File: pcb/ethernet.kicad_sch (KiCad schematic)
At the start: 39 parts, among them J6 RJ45_Hanrun_HR911105A_Horizon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, U7 W5500, Y1 Crystal_GND24

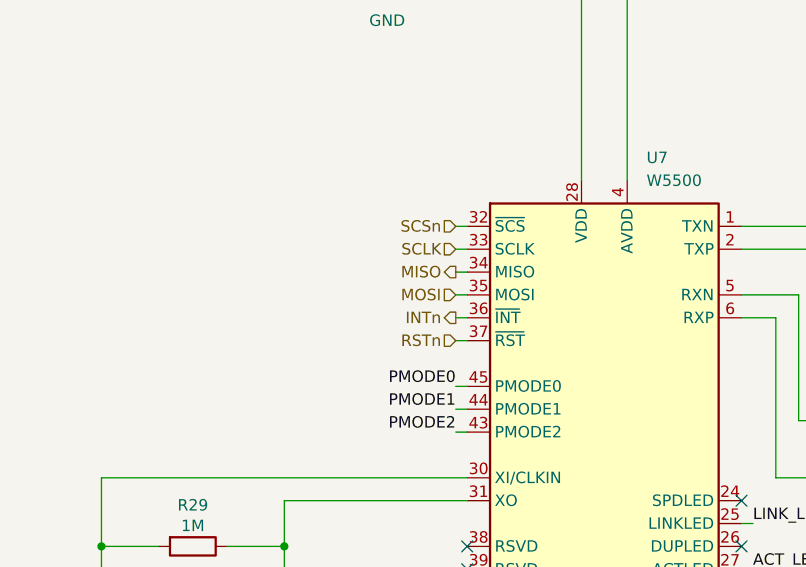
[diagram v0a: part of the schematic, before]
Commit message: feat: connect ethernet to mcu and sort erc errors
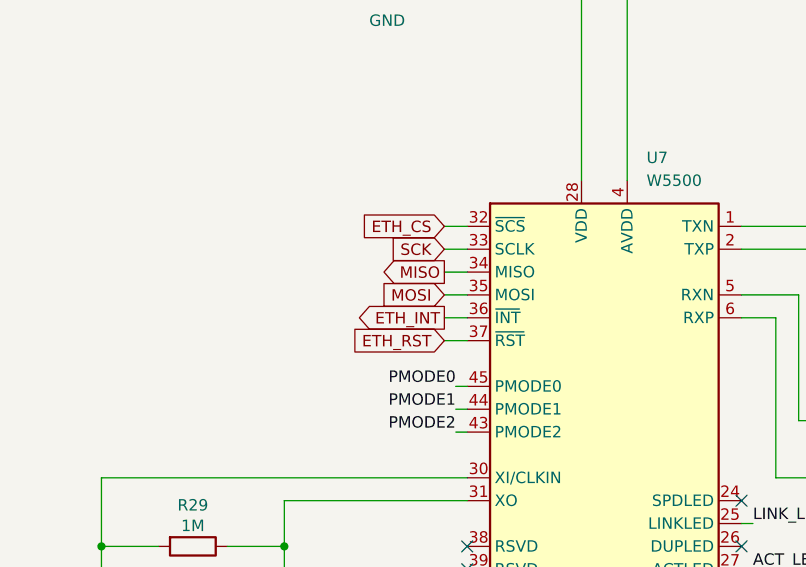
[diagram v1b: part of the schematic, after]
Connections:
- net INTn renamed ETH_INT
- net RSTn renamed ETH_RST
- net SCLK renamed SCK
- net SCSn renamed ETH_CS
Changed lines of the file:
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@@
-	(wire
-		(pts
-			(xy 67.31 76.2) (xy 68.58 76.2)
-		)
-		(stroke
-			(width 0)
-			(type default)
-		)
-	)
-	(wire
-		(pts
-			(xy 67.31 81.28) (xy 68.58 81.28)
-		)
-		(stroke
-			(width 0)
-			(type default)
-		)
-	)
 	(wire
 		(pts
@@
 	(wire
 		(pts
-			(xy 67.31 71.12) (xy 68.58 71.12)
-		)
-		(stroke
-			(width 0)
-			(type default)
-		)
-	)
-	(wire
-		(pts
 			(xy 132.08 173.99) (xy 133.35 173.99)
 		)
@@
 	(wire
 		(pts
+			(xy 66.04 78.74) (xy 68.58 78.74)
+		)
+		(stroke
+			(width 0)
+			(type default)
+		)
+	)
+	(wire
+		(pts
 			(xy 129.54 96.52) (xy 133.35 96.52)
 		)
@@
 	(wire
 		(pts
+			(xy 66.04 73.66) (xy 68.58 73.66)
+		)
+		(stroke
+			(width 0)
+			(type default)
+		)
+	)
+	(wire
+		(pts
 			(xy 86.36 29.21) (xy 86.36 63.5)
 		)
@@
 	(wire
 		(pts
-			(xy 67.31 78.74) (xy 68.58 78.74)
-		)
-		(stroke
-			(width 0)
-			(type default)
-		)
-	)
-	(wire
-		(pts
 			(xy 134.62 38.1) (xy 134.62 39.37)
 		)
@@
 	(wire
 		(pts
+			(xy 66.04 68.58) (xy 68.58 68.58)
+		)
+		(stroke
+			(width 0)
+			(type default)
+		)
+	)
+	(wire
+		(pts
+			(xy 66.04 71.12) (xy 68.58 71.12)
+		)
+		(stroke
+			(width 0)
+			(type default)
+		)
+	)
+	(wire
+		(pts
 			(xy 134.62 39.37) (xy 121.92 39.37)
 		)
@@
 	(wire
 		(pts
+			(xy 66.04 76.2) (xy 68.58 76.2)
+		)
+		(stroke
+			(width 0)
+			(type default)
+		)
+	)
+	(wire
+		(pts
 			(xy 99.06 101.6) (xy 100.33 101.6)
 		)
@@
 	(wire
 		(pts
-			(xy 67.31 68.58) (xy 68.58 68.58)
-		)
-		(stroke
-			(width 0)
-			(type default)
-		)
-	)
-	(wire
-		(pts
 			(xy 241.3 71.12) (xy 246.38 71.12)
 		)
@@
 	(wire
 		(pts
-			(xy 67.31 73.66) (xy 68.58 73.66)
-		)
-		(stroke
-			(width 0)
-			(type default)
-		)
-	)
-	(wire
-		(pts
 			(xy 111.76 128.27) (xy 111.76 129.54)
 		)
@@
 		(pts
 			(xy 144.78 55.88) (xy 144.78 57.15)
+		)
+		(stroke
+			(width 0)
+			(type default)
+		)
+	)
+	(wire
+		(pts
+			(xy 66.04 81.28) (xy 68.58 81.28)
 		)
 		(stroke
@@
 		)
 	)
-	(hierarchical_label "INTn"
+	(global_label "MISO"
 		(shape output)
-		(at 67.31 78.74 180)
+		(at 66.04 73.66 180)
+		(fields_autoplaced yes)
 		(effects
 			(font
@@
 			(justify right)
 		)
-	)
-	(hierarchical_label "SCSn"
+		(property "Intersheetrefs" "${INTERSHEET_REFS}"
+			(at 58.4586 73.66 0)
+			(hide yes)
+			(show_name no)
+			(do_not_autoplace no)
+			(effects
+				(font
+					(size 1.27 1.27)
+				)
+				(justify right)
+			)
+		)
+	)
+	(global_label "ETH_RST"
 		(shape input)
-		(at 67.31 68.58 180)
+		(at 66.04 81.28 180)
+		(fields_autoplaced yes)
 		(effects
 			(font
@@
 			(justify right)
 		)
-	)
-	(hierarchical_label "MISO"
-		(shape output)
-		(at 67.31 73.66 180)
+		(property "Intersheetrefs" "${INTERSHEET_REFS}"
+			(at 55.193 81.28 0)
+			(hide yes)
+			(show_name no)
+			(do_not_autoplace no)
+			(effects
+				(font
+					(size 1.27 1.27)
+				)
+				(justify right)
+			)
+		)
+	)
+	(global_label "MOSI"
+		(shape input)
+		(at 66.04 76.2 180)
+		(fields_autoplaced yes)
 		(effects
 			(font
@@
 			(justify right)
 		)
-	)
-	(hierarchical_label "SCLK"
+		(property "Intersheetrefs" "${INTERSHEET_REFS}"
+			(at 58.4586 76.2 0)
+			(hide yes)
+			(show_name no)
+			(do_not_autoplace no)
+			(effects
+				(font
+					(size 1.27 1.27)
+				)
+				(justify right)
+			)
+		)
+	)
+	(global_label "ETH_CS"
 		(shape input)
-		(at 67.31 71.12 180)
+		(at 66.04 68.58 180)
+		(fields_autoplaced yes)
 		(effects
 			(font
@@
 			(justify right)
 		)
-	)
-	(hierarchical_label "MOSI"
+		(property "Intersheetrefs" "${INTERSHEET_REFS}"
+			(at 56.1606 68.58 0)
+			(hide yes)
+			(show_name no)
+			(do_not_autoplace no)
+			(effects
+				(font
+					(size 1.27 1.27)
+				)
+				(justify right)
+			)
+		)
+	)
+	(global_label "SCK"
 		(shape input)
-		(at 67.31 76.2 180)
+		(at 66.04 71.12 180)
+		(fields_autoplaced yes)
 		(effects
 			(font
@@
 			(justify right)
 		)
-	)
-	(hierarchical_label "RSTn"
-		(shape input)
-		(at 67.31 81.28 180)
+		(property "Intersheetrefs" "${INTERSHEET_REFS}"
+			(at 59.3053 71.12 0)
+			(hide yes)
+			(show_name no)
+			(do_not_autoplace no)
+			(effects
+				(font
+					(size 1.27 1.27)
+				)
+				(justify right)
+			)
+		)
+	)
+	(global_label "ETH_INT"
+		(shape output)
+		(at 66.04 78.74 180)
+		(fields_autoplaced yes)
 		(effects
 			(font
@@
 			(justify right)
 		)
-	)
+		(property "Intersheetrefs" "${INTERSHEET_REFS}"
+			(at 55.7372 78.74 0)
+			(hide yes)
+			(show_name no)
+			(do_not_autoplace no)
+			(effects
+				(font
+					(size 1.27 1.27)
+				)
+				(justify right)
+			)
+		)
+	)

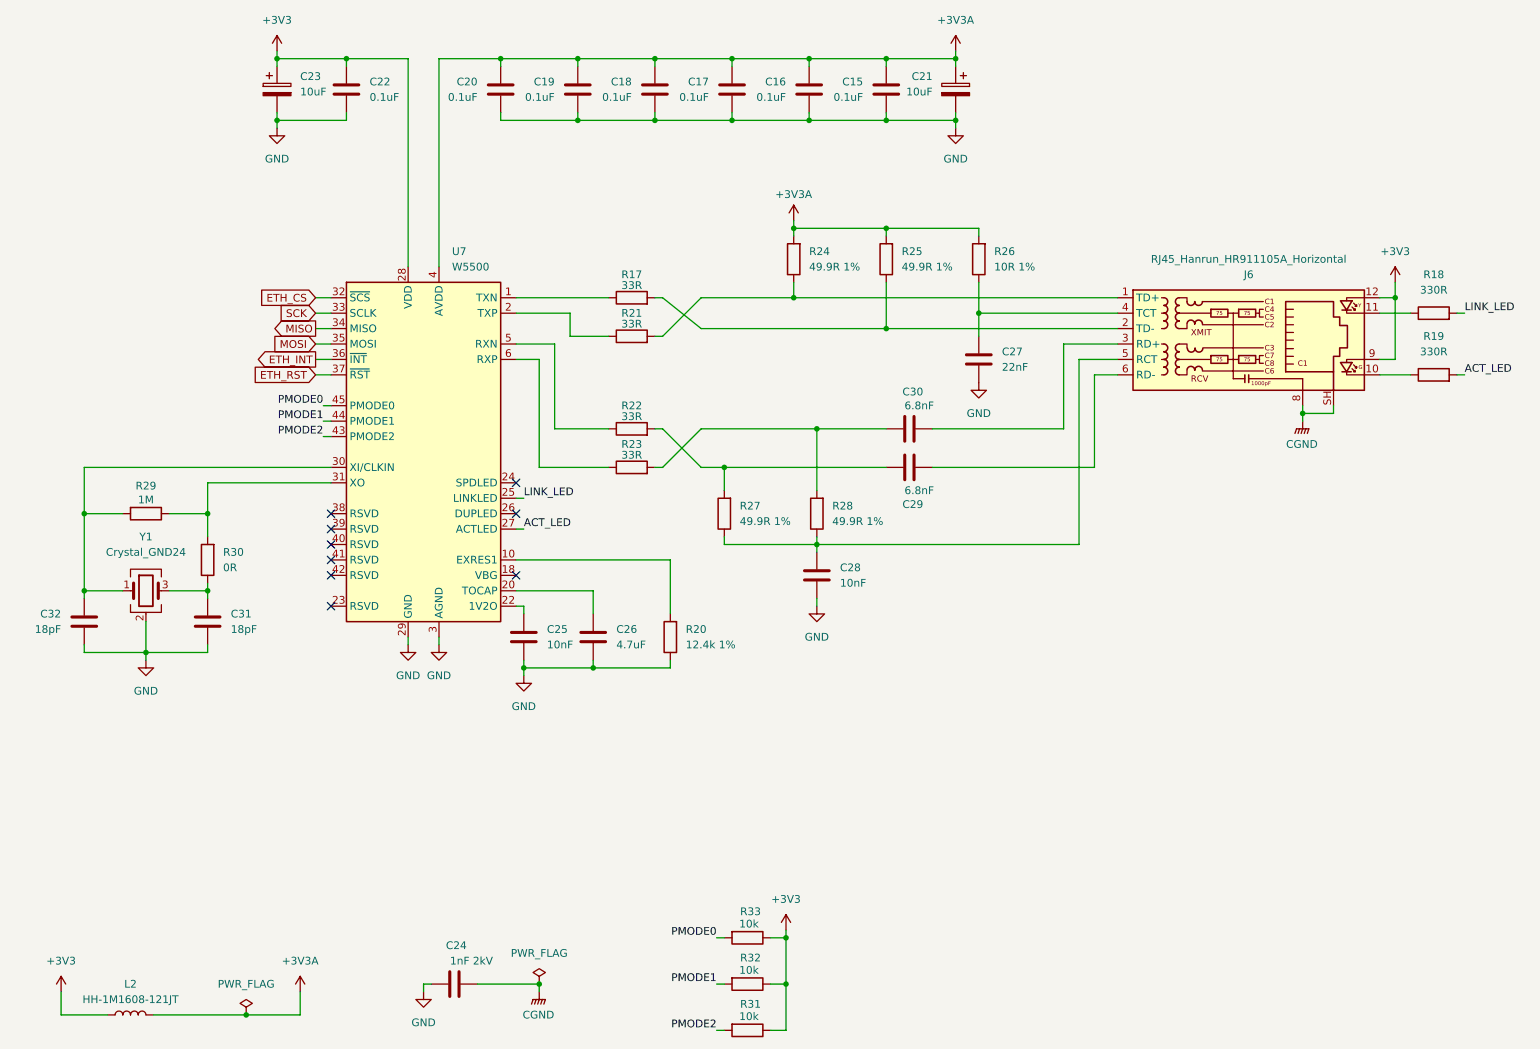
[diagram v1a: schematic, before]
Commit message: feat: update compoents with lcsc parts
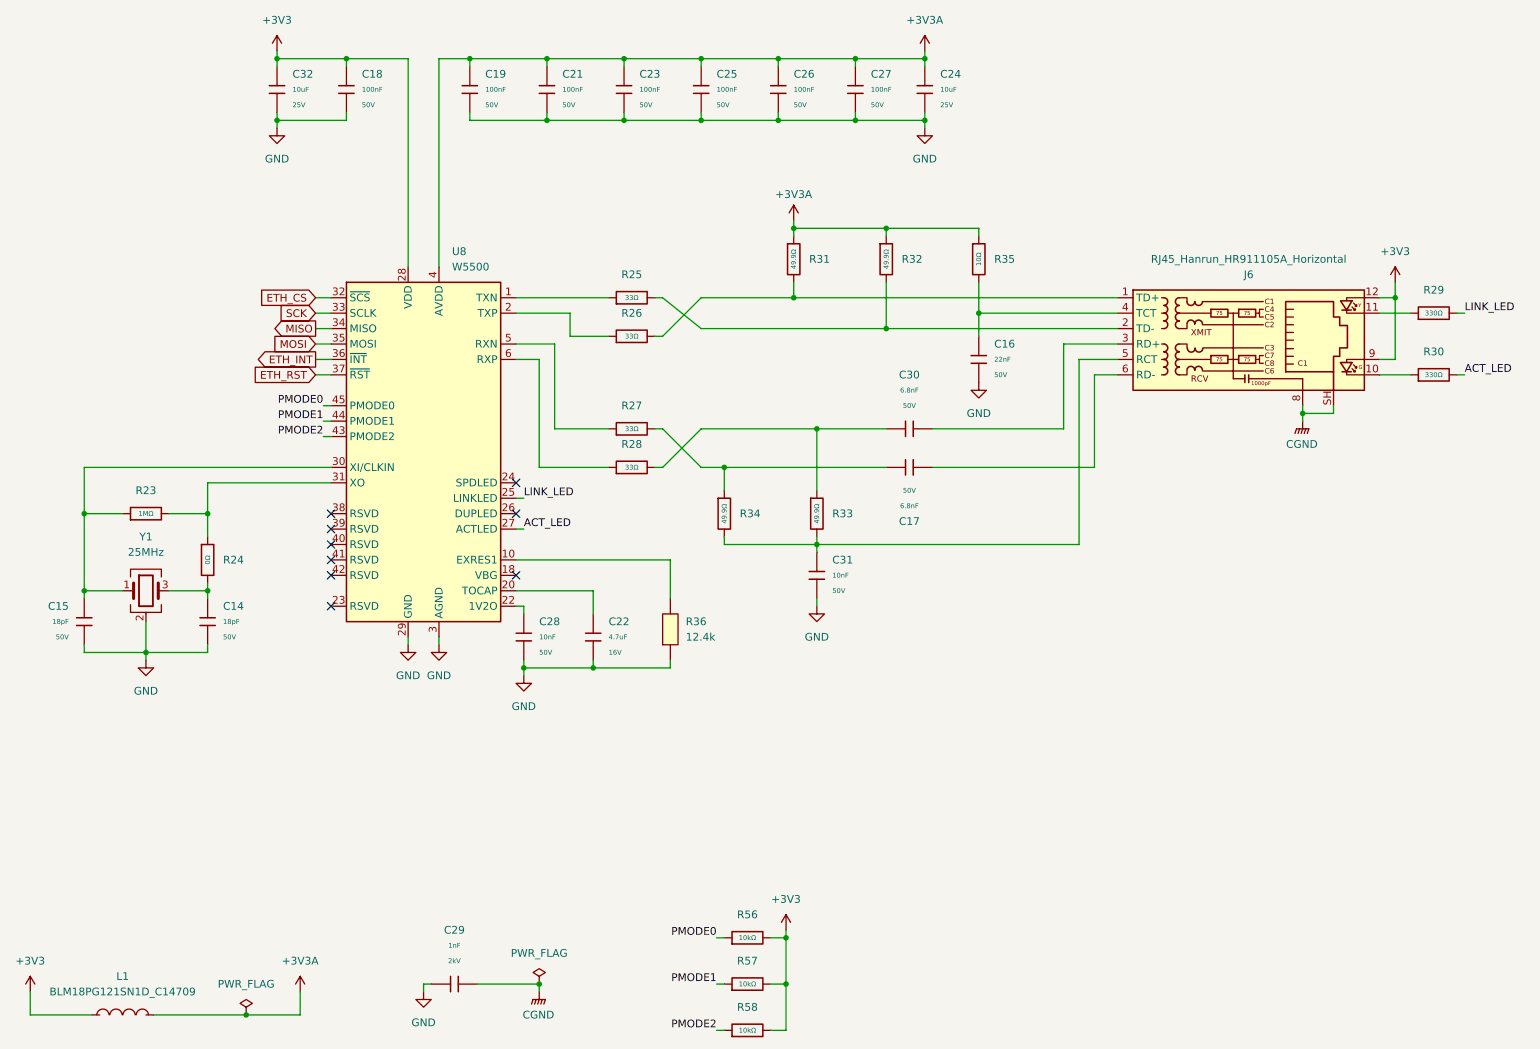
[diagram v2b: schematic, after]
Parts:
- removed C15, C16, C17, C18, C19, C20, C22: 0.1uF, symbol Device:C
- removed C21, C23: 10uF, symbol Device:C_Polarized
- removed C24: 1nF 2kV, symbol Device:C
- removed C25, C28: 10nF, symbol Device:C
- removed C26: 4.7uF, symbol Device:C
- removed C27: 22nF, symbol Device:C
- removed C29, C30: 6.8nF, symbol Device:C
- removed C31, C32: 18pF, symbol Device:C
- removed L2: HH-1M1608-121JT, symbol Device:L
- removed R17, R21, R22, R23: 33R, symbol Device:R
- removed R18, R19: 330R, symbol Device:R
- removed R20: 12.4k 1%, symbol Device:R
- removed R24, R25, R27, R28: 49.9R 1%, symbol Device:R
- removed R26: 10R 1%, symbol Device:R
- removed R29: 1M, symbol Device:R
- removed R30: 0R, symbol Device:R
- removed R31, R32, R33: 10k, symbol Device:R
- added C14, C15: 18pF, PCM_JLCPCB:C_0603, symbol PCM_JLCPCB-Capacitors:0603,18pF
- added C16: 22nF, PCM_JLCPCB:C_0603, symbol PCM_JLCPCB-Capacitors:0603,22nF
- added C17, C30: 6.8nF, PCM_JLCPCB:C_0603, symbol PCM_JLCPCB-Capacitors:0603,6.8nF
- added C18, C19, C21, C23, C25, C26, C27: 100nF, PCM_JLCPCB:C_0603, symbol PCM_JLCPCB-Capacitors:0603,100nF
- added C22: 4.7uF, PCM_JLCPCB:C_0603, symbol PCM_JLCPCB-Capacitors:0603,4.7uF
- added C24, C32: 10uF, PCM_JLCPCB:C_0603, symbol PCM_JLCPCB-Capacitors:0603,10uF,(2)
- added C28, C31: 10nF, PCM_JLCPCB:C_0603, symbol PCM_JLCPCB-Capacitors:0603,10nF
- added C29: 1nF, PCM_JLCPCB:C_1206, symbol PCM_JLCPCB-Capacitors:1206,1nF
- added L1: BLM18PG121SN1D_C14709, EasyEDA:L0603, symbol EasyEDA:BLM18PG121SN1D_C14709
- added R23: 1MΩ, PCM_JLCPCB:R_0603, symbol PCM_JLCPCB-Resistors:0603,1MΩ
- added R24: 0Ω, PCM_JLCPCB:R_0603, symbol PCM_JLCPCB-Resistors:0603,0Ω
- added R25, R26, R27, R28: 33Ω, PCM_JLCPCB:R_0603, symbol PCM_JLCPCB-Resistors:0603,33Ω
- added R29, R30: 330Ω, PCM_JLCPCB:R_0603, symbol PCM_JLCPCB-Resistors:0603,330Ω
- added R31, R32, R33, R34: 49.9Ω, PCM_JLCPCB:R_0603, symbol PCM_JLCPCB-Resistors:0603,49.9Ω
- added R35: 10Ω, PCM_JLCPCB:R_0603, symbol PCM_JLCPCB-Resistors:0603,10Ω
- added R36: 12.4k, EasyEDA:R0603, symbol EasyEDA:FRC0603F1242TS
- added R56, R57, R58: 10kΩ, PCM_JLCPCB:R_0603, symbol PCM_JLCPCB-Resistors:0603,10kΩ
- J6: footprint Connector_RJ:RJ45_Hanrun_HR911105A_Horizontal -> EasyEDA:RJ45-TH_HR911105A; LCSC Part (none) -> C12074; MPN (none) -> HR911105A
- U8: renamed from U7; footprint Package_QFP:LQFP-48_7x7mm_P0.5mm -> EasyEDA:LQFP-48_L7.0-W7.0-P0.50-LS9.0-BL; LCSC Part (none) -> C32843; MPN (none) -> W5500
- Y1: value Crystal_GND24 -> 25MHz; footprint (none) -> PCM_JLCPCB:OSC-SMD_4P-L3.2-W2.5-BL; LCSC Part (none) -> C9006; MPN (none) -> X322525MOB4SI
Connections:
- net +3V3: now also C18.1, C32.1, L1.1, R56.2, R57.2, R58.2
- net +3V3A: now also C19.1, C21.1, C23.1, C24.1, C25.1, C26.1, C27.1, L1.2, R31.1, R32.1, R35.1
- net ACT_LED: now also R30.2
- net CGND: now also C29.2
- net GND: now also C14.2, C15.2, C16.2, C18.2, C19.2, C21.2, C22.2, C23.2, C24.2, C25.2, C26.2, C27.2, C28.2, C29.1, C31.2, C32.2, R36.1
- net LINK_LED: now also R29.2
- net PMODE0: now also R56.1
- net PMODE1: now also R57.1
- net PMODE2: now also R58.1
- net at U8.6 (RXP): now also R28.1
- net at Y1.3: now also C14.1, R24.2
- net at U8.31 (XO): now also R23.2, R24.1
- net at J6.5 (RCT): now also C31.1, R33.2, R34.2
- net at J6.4 (TCT): now also C16.1, R35.2
- net at J6.2 (TD-): now also R25.2, R32.2
- net at U8.1 (TXN): now also R25.1
- net at J6.6 (RD-): now also C17.2
- net at J6.10: now also R30.1
- net at U8.20 (TOCAP): now also C22.1
- net at J6.1 (TD+): now also R26.2, R31.2
- net at J6.11: now also R29.1
- net at J6.3 (RD+): now also C30.2
- net at U8.5 (RXN): now also R27.1
- net at U8.30 (XI/CLKIN), Y1.1: now also C15.1, R23.1
- net at U8.10 (EXRES1): now also R36.2
- net at U8.2 (TXP): now also R26.1
- net at U8.22 (1V2O): now also C28.1
- new net: C17.1, R27.2, R34.1
- new net: C30.1, R28.2, R33.1

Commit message: feat: layout meterbus frontend
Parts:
- renumbered C15 to C17, C14 to C18, C32 to C19, C18 to C20, C29 to C21, C19 to C22, C28 to C23, C21 to C24, C22 to C25, C23 to C26, C25 to C27, C26 to C28, C31 to C29, C27 to C30, C30 to C31, C17 to C32, C24 to C33, C16 to C34, J6 to J4, L1 to L2, R23 to R31, R24 to R32, R25 to R33, R26 to R34, R27 to R35, R28 to R36, R36 to R37, R34 to R38, R56 to R39, R57 to R40, R58 to R41, R31 to R42, R33 to R43, R32 to R44, R35 to R45, R29 to R46, R30 to R47, U8 to U9

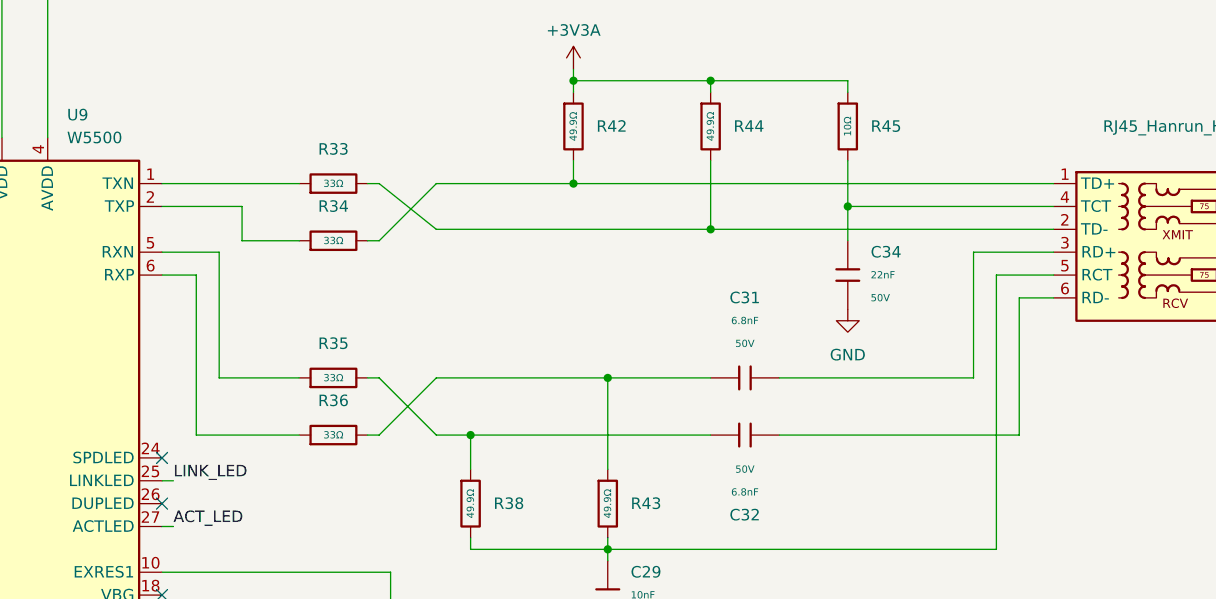
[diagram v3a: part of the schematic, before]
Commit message: feat: layout ethernet
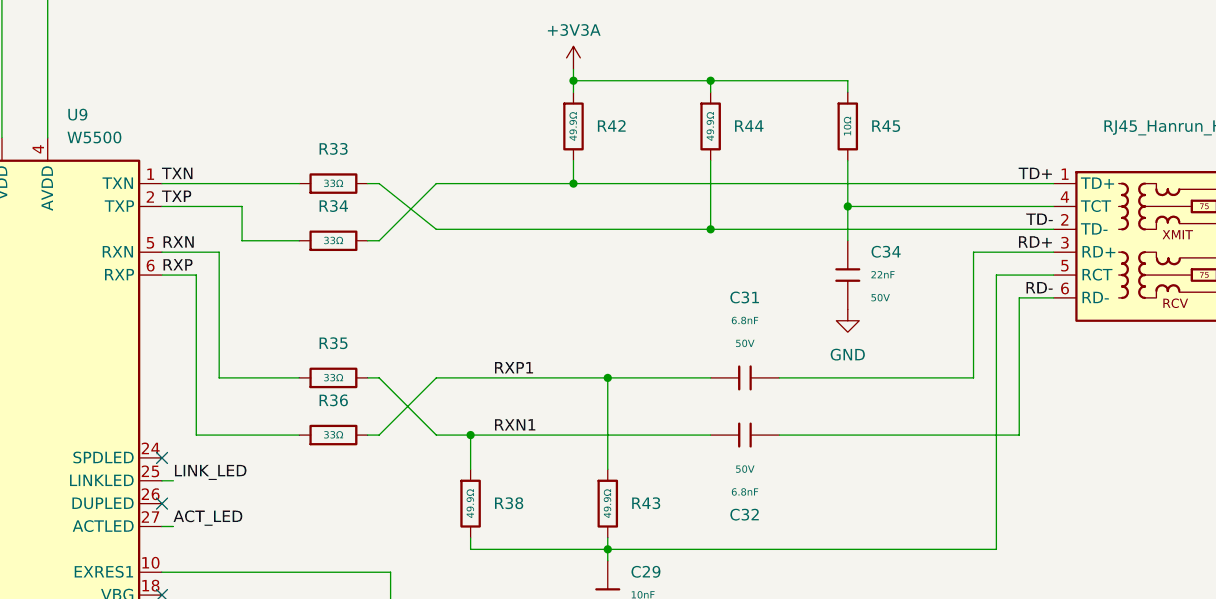
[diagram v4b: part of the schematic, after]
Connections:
- net RXN: now reaches R35.1, U9.5 (RXN)
- net RXN1: now reaches C32.1, R35.2, R38.1
- net RD-: now reaches C32.2, J4.6 (RD-)
- net TXN: now reaches R33.1, U9.1 (TXN)
- net TD-: now reaches J4.2 (TD-), R33.2, R44.2
- net RXP: now reaches R36.1, U9.6 (RXP)
- net RXP1: now reaches C31.1, R36.2, R43.1
- net TD+: now reaches J4.1 (TD+), R34.2, R42.2
- net RD+: now reaches C31.2, J4.3 (RD+)
- net TXP: now reaches R34.1, U9.2 (TXP)
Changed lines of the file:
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@@
+		)
+	)
+	(label "RXP1"
+		(at 135.89 90.17 0)
+		(effects
+			(font
+				(size 1.27 1.27)
+			)
+			(justify left bottom)
+		)
+	)
+	(label "TXN"
+		(at 99.06 68.58 0)
+		(effects
+			(font
+				(size 1.27 1.27)
+			)
+			(justify left bottom)
+		)
+	)
+	(label "RXN1"
+		(at 135.89 96.52 0)
+		(effects
+			(font
+				(size 1.27 1.27)
+			)
+			(justify left bottom)
+		)
+	)
+	(label "TXP"
+		(at 99.06 71.12 0)
+		(effects
+			(font
+				(size 1.27 1.27)
+			)
+			(justify left bottom)
+		)
+	)
+	(label "TD-"
+		(at 198.12 73.66 180)
+		(effects
+			(font
+				(size 1.27 1.27)
+			)
+			(justify right bottom)
 		)
 	)
@@
 		)
 	)
+	(label "RXN"
+		(at 99.06 76.2 0)
+		(effects
+			(font
+				(size 1.27 1.27)
+			)
+			(justify left bottom)
+		)
+	)
 	(label "ACT_LED"
 		(at 100.33 106.68 0)
@@
 	(label "PMODE2"
 		(at 67.31 91.44 180)
+		(effects
+			(font
+				(size 1.27 1.27)
+			)
+			(justify right bottom)
+		)
+	)
+	(label "RD+"
+		(at 198.12 76.2 180)
 		(effects
 			(font
@@
 		)
 	)
+	(label "TD+"
+		(at 198.12 68.58 180)
+		(effects
+			(font
+				(size 1.27 1.27)
+			)
+			(justify right bottom)
+		)
+	)
 	(label "ACT_LED"
 		(at 255.27 81.28 0)
@@
 		)
 	)
+	(label "RXP"
+		(at 99.06 78.74 0)
+		(effects
+			(font
+				(size 1.27 1.27)
+			)
+			(justify left bottom)
+		)
+	)
+	(label "RD-"
+		(at 198.12 81.28 180)
+		(effects
+			(font
+				(size 1.27 1.27)
+			)
+			(justify right bottom)
+		)
+	)
